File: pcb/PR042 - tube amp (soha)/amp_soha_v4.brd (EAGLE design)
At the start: 82 x 48.9 mm, 59 parts, among them IC1 NE5532, IC2 7812, IC3 7912, Q1 J113, Q2 J113, Q3 J113, Q4 J113

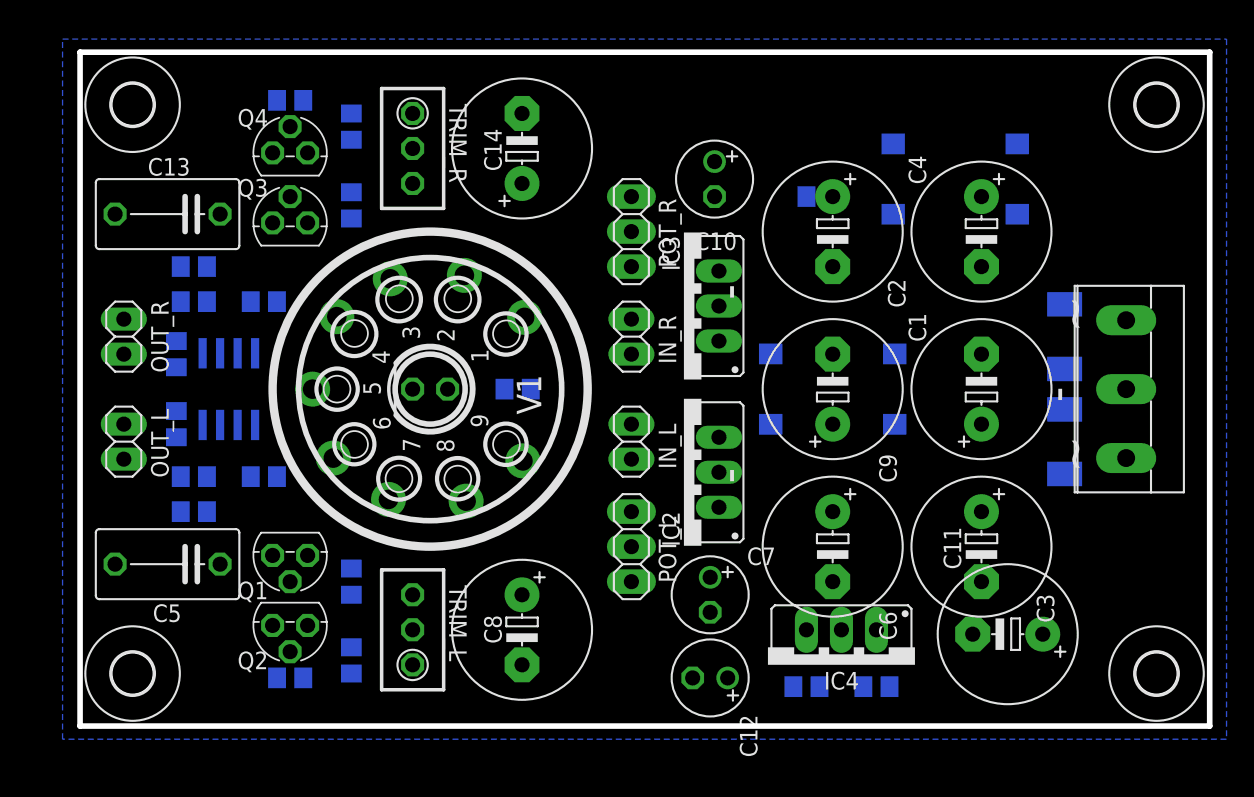
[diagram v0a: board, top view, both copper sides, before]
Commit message: 
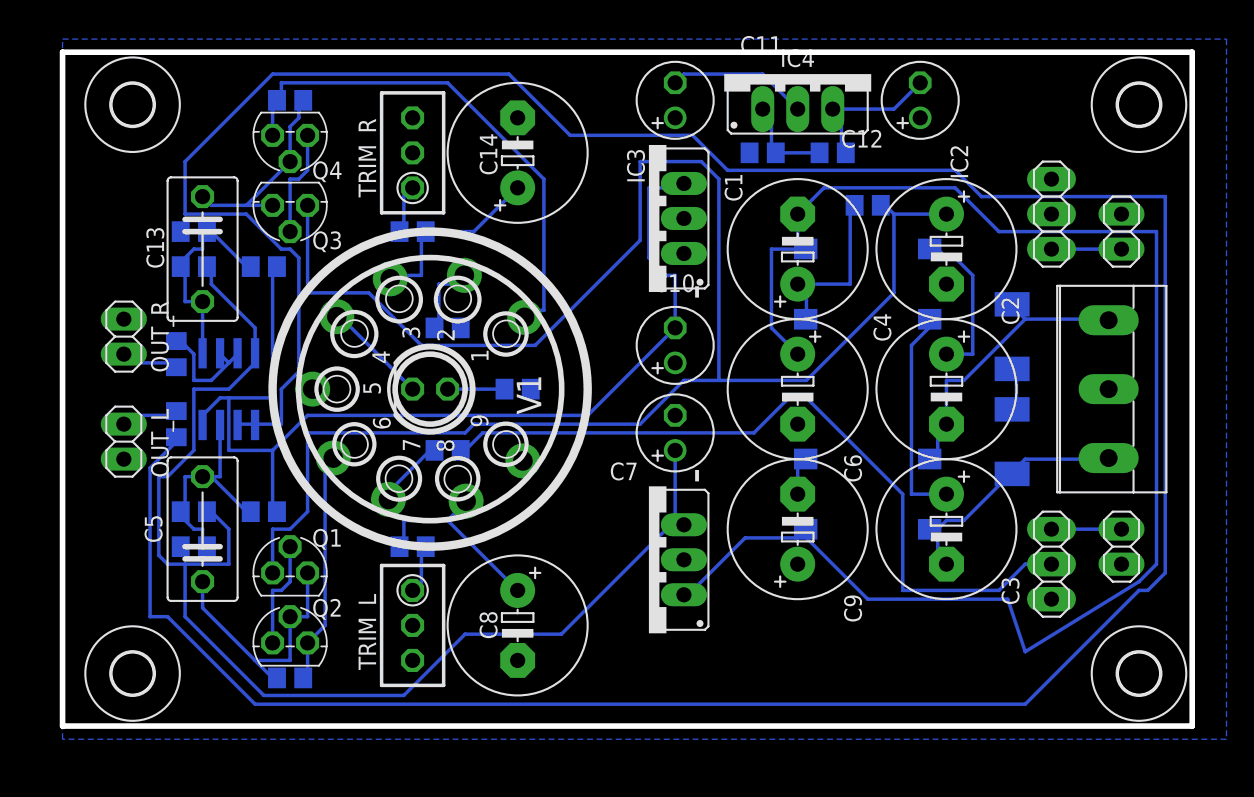
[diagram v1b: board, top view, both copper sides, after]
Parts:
- C11: value 470uF/35V -> 47uF/35V; device amp_soha:E5-10,5 -> amp_soha:E2,5-6
- moved C11 45.6 mm to (45.7, 46.4), turned to 90 degrees
- moved C12 44.6 mm to (63.5, 46.4), turned to 90 degrees
- moved IC4 43.0 mm to (54.6, 48.3), turned to 0 degrees
- moved R11 39.6 mm to (52.1, 42.5), turned to 180 degrees
- moved R9 38.8 mm to (57.1, 42.5), turned to 180 degrees
- moved IN_L 36.4 mm to (78.1, 14.0)
- moved IN_R 36.4 mm to (78.1, 36.8)
- moved POT_L 30.5 mm to (73.0, 12.7)
- moved POT_R 30.5 mm to (73.0, 38.1)
- moved C1 16.8 mm to (54.6, 35.6)
- moved R16 16.2 mm to (29.2, 29.8), turned to 180 degrees
- moved C10 12.4 mm to (45.7, 28.6), turned to 90 degrees
- moved C7 12.0 mm to (45.7, 22.2), turned to 90 degrees
- moved R6 11.8 mm to (29.2, 21.0), turned to 180 degrees
- moved C4 11.7 mm to (65.4, 25.4)
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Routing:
- net N$24: track 0.00 -> 228.0 mm
- net +24V: track 0.00 -> 131.2 mm
- net N$6: track 0.00 -> 109.5 mm
- net +12V: track 0.00 -> 91.1 mm
- net -12V: track 0.00 -> 75.0 mm
- net N$13: track 0.00 -> 55.1 mm
- net N$21: track 0.00 -> 37.7 mm
- net N$2: track 0.00 -> 21.6 mm
- net N$16: track 0.00 -> 19.6 mm
- net N$1: track 0.00 -> 18.5 mm
- net -12.6V: track 0.00 -> 18.3 mm
- net N$22: track 0.00 -> 17.4 mm
- net N$19: track 0.00 -> 17.3 mm
- net N$34: track 0.00 -> 16.4 mm
- net N$8: track 0.00 -> 15.8 mm
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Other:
- board text removed: "~"

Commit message: 
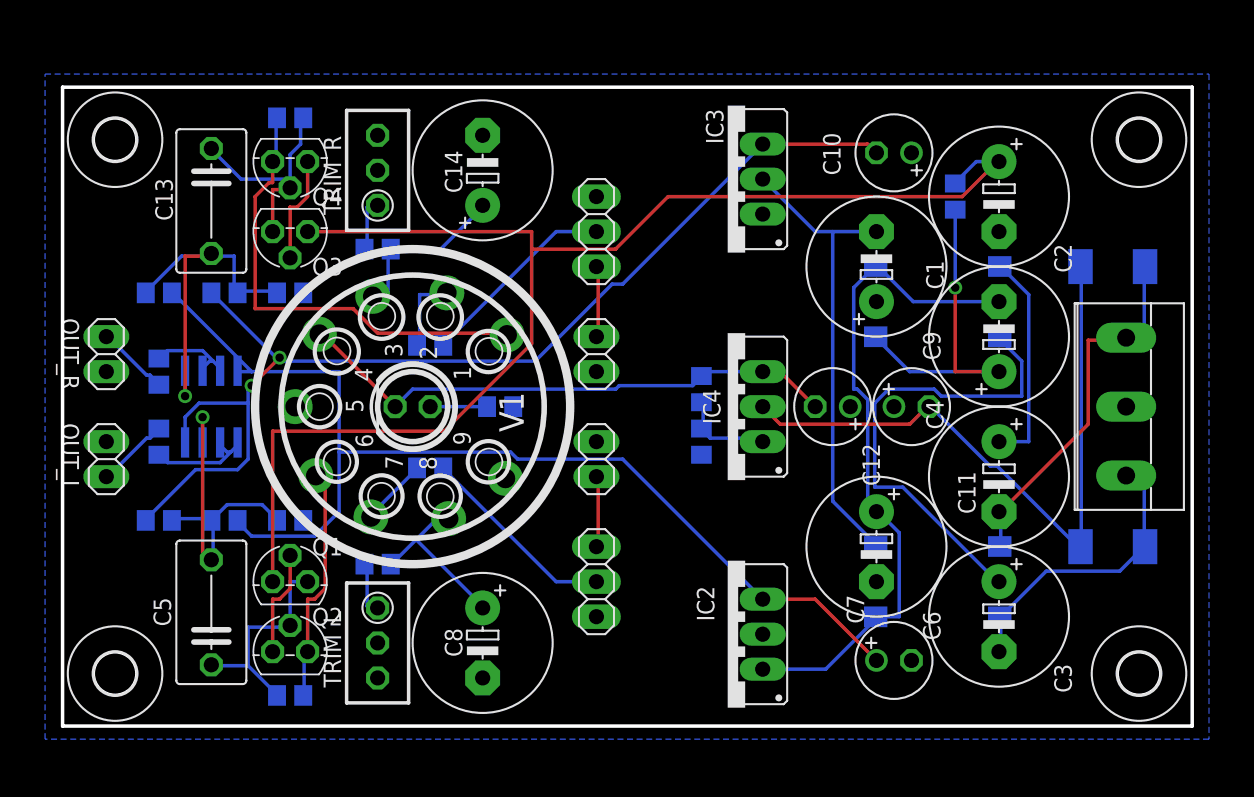
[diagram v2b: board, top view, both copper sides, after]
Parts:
- moved IN_R 39.1 mm to (40.0, 27.9), turned to 270 degrees
- moved IN_L 38.6 mm to (40.0, 20.3), turned to 90 degrees
- moved POT_L 33.0 mm to (40.0, 11.4)
- moved POT_R 33.0 mm to (40.0, 36.8)
- moved C11 28.1 mm to (62.9, 24.1), turned to 0 degrees
- moved IC4 24.7 mm to (49.5, 24.1), turned to 90 degrees
- moved C12 23.1 mm to (57.1, 24.1), turned to 180 degrees
- moved C7 22.9 mm to (61.6, 5.71), turned to 0 degrees
- moved R11 21.4 mm to (47.6, 21.6), turned to 90 degrees
- moved C10 21.1 mm to (61.6, 42.5), turned to 180 degrees
- moved C9 19.9 mm to (60.3, 34.3)
- moved R9 19.6 mm to (47.6, 25.4), turned to 90 degrees
- moved C1 15.9 mm to (69.2, 29.2)
- moved C6 12.8 mm to (60.3, 14.0)
- moved D3 10.6 mm to (77.5, 14.0), turned to 0 degrees
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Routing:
- net N$24: track 228.0 -> 7.83 mm
- net N$6: track 109.5 -> 49.6 mm
- net N$13: track 55.1 -> 14.6 mm
- net N$3: track 13.5 -> 48.8 mm
- net +24V: track 131.2 -> 97.1 mm
- net N$5: track 3.12 -> 34.0 mm
- net -12.6V: track 18.3 -> 40.3 mm
- net N$8: track 15.8 -> 34.2 mm
- net N$27: track 0.00 -> 14.6 mm
- net N$11: track 12.4 -> 24.9 mm, vias 0 -> 1
- net +12V: track 91.1 -> 79.6 mm
- net N$34: track 16.4 -> 27.6 mm, vias 0 -> 1
- net -12V: track 75.0 -> 81.9 mm, vias 0 -> 2
- net N$22: track 17.4 -> 24.4 mm, vias 0 -> 1
- net N$2: track 21.6 -> 27.2 mm
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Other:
- board size 82 x 48.9 mm -> 82 x 46.4 mm
- board text removed: "-"

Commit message: 
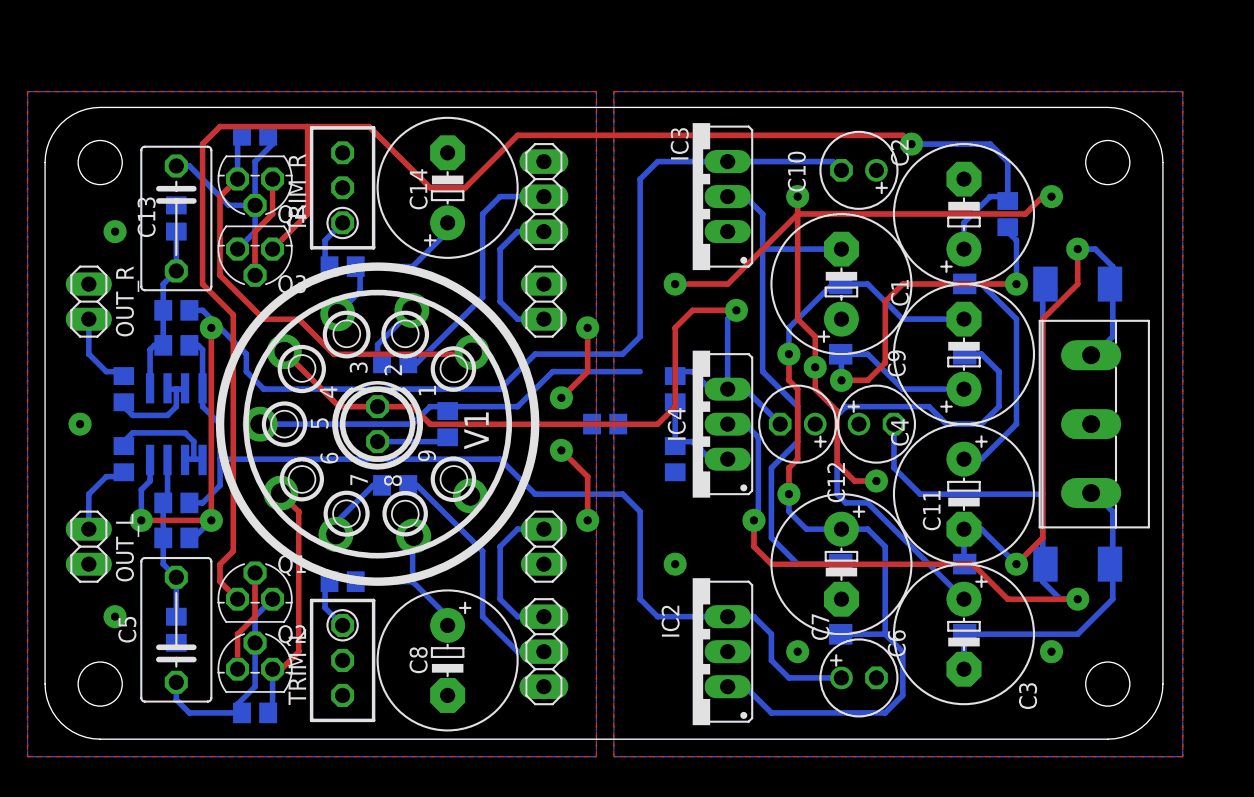
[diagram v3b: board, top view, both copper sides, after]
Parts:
- removed U$1, U$2, U$3, U$4: (no value), amp_soha:3,0
- added R5: 0, amp_soha:R0805
- moved R4 11.5 mm to (9.53, 7.94), turned to 270 degrees
- moved R14 9.86 mm to (9.53, 37.8), turned to 90 degrees
- moved IN_L 7.41 mm to (36.2, 14.0), turned to 270 degrees
- moved OUT_L 6.48 mm to (3.17, 14.0), turned to 270 degrees
- moved POT_L 6.35 mm to (36.2, 6.35)
- moved IN_R 5.39 mm to (36.2, 31.8), turned to 90 degrees
- moved POT_R 4.58 mm to (36.2, 39.4)
- moved R10 4.02 mm to (29.2, 22.9), turned to 270 degrees
- moved D5 4.02 mm to (9.53, 28.6)
- moved OUT_R 4.02 mm to (3.17, 31.8), turned to 90 degrees
- moved R1 4.02 mm to (69.8, 38.1)
- moved D1 3.72 mm to (9.53, 17.1)
- moved D6 3.72 mm to (9.53, 31.1), turned to 0 degrees
- moved C3 2.84 mm to (66.7, 7.62)
- moved C6 2.84 mm to (57.8, 12.7)
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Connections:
- new net GND: C10.+, C11.+, C12.+, C2.-, C6.-, C7.-, C9.+, IC2.GND, IC3.GND, R10.1, R11.1, R5.2, V1.5, X1.2
- net AGND: now also R5.1; no longer C10.+, C11.+, C12.+, C2.-, C6.-, C7.-, C9.+, IC2.GND, IC3.GND, R10.1, R11.1, V1.5, X1.2
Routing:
- net GND: track 0.00 -> 83.5 mm, vias 0 -> 8
- net N$3: track 48.8 -> 75.6 mm, vias 0 -> 2
- net +24V: track 97.1 -> 116.7 mm, vias 0 -> 1
- net -12.6V: track 40.3 -> 57.1 mm, vias 0 -> 1
- net N$6: track 49.6 -> 66.1 mm, vias 0 -> 2
- net N$2: track 27.2 -> 43.1 mm, vias 0 -> 2
- net N$34: track 27.6 -> 13.3 mm, vias 1 -> 0
- net AGND: track 0.47 -> 11.9 mm, vias 0 -> 7
- net N$22: track 24.4 -> 13.0 mm, vias 1 -> 0
- net N$11: track 24.9 -> 34.5 mm, vias 1 -> 2
- net -12V: track 81.9 -> 90.7 mm, vias 2 -> 3
- net +12V: track 79.6 -> 71.2 mm
- net N$5: track 34.0 -> 40.2 mm
- net N$26: track 5.33 -> 11.2 mm
- net N$12: track 5.33 -> 11.2 mm
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- added copper zone on layer 1, net AGND
- added copper zone on layer 1, net GND
- added copper zone on layer 16, net GND
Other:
- board size 82 x 46.4 mm -> 81.1 x 45.8 mm
- board text added: "4.0mm"
- board text added: "56mm"
- board text added: "90mm"
- board text added: "D = 3.2mm"
- board text added: "R = 4.0mm"

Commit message: 
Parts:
- removed TRIM_R: 2k, amp_soha:RTRIM3296W
- added R15: 300, amp_soha:R0805
- R16: value 300 -> 560
- R17: value 560 -> 2k; device amp_soha:R0805 -> amp_soha:RTRIM3296W
- R5: value 0 -> 300
- R6: value 300 -> SHORT; device amp_soha:R0805 -> amp_soha:SHORT
- moved IN_L 17.8 mm to (36.2, 31.8), turned to 90 degrees
- moved IN_R 17.8 mm to (36.2, 14.0), turned to 270 degrees
- moved OUT_L 17.8 mm to (3.17, 31.8), turned to 90 degrees
- moved OUT_R 17.8 mm to (3.17, 14.0), turned to 270 degrees
- moved R5 15.9 mm to (25.4, 18.4)
- moved R6 15.9 mm to (40.6, 22.9), turned to 0 degrees
- moved R16 7.96 mm to (21.6, 34.3), turned to 0 degrees
- moved R17 5.72 mm to (21.6, 40.0), flipped to the top
- renumbered TRIM_L to R8
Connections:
- net AGND: now also R17.2, R17.3, R6.2; no longer R5.1, TRIM_R.2, TRIM_R.3
- net GND: now also R6.1; no longer R5.2
- net N$10: now also R15.1; no longer R16.1
- net N$12: now also IN_R.1; no longer IN_L.1
- net N$13: now also R5.2; no longer R6.2
- net N$14: now also R5.1; no longer R6.1
- net N$18: now also R16.2, R17.1; no longer R17.2, TRIM_R.1
- net N$25: now also OUT_R.1; no longer OUT_L.1
- net N$26: now also IN_L.1; no longer IN_R.1
- net N$27: now also R15.2; no longer R16.2
- net N$29: now also R16.1; no longer R17.1
- net N$36: now also OUT_L.1; no longer OUT_R.1
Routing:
- net AGND: track 11.9 -> 22.0 mm
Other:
- board text added: "+"
- board text added: "-"
- board text added: "L"
- board text added: "R"
